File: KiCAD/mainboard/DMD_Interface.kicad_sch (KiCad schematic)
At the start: 21 parts, among them IC3 SN74AUP1G06DCKR, IC4 SN74AUP1G07DCKR, IC5 SN74AUP1G07DCKR, J1 AXT550124, J10 Conn_01x05_Pin, J30 Conn_01x08_Pin

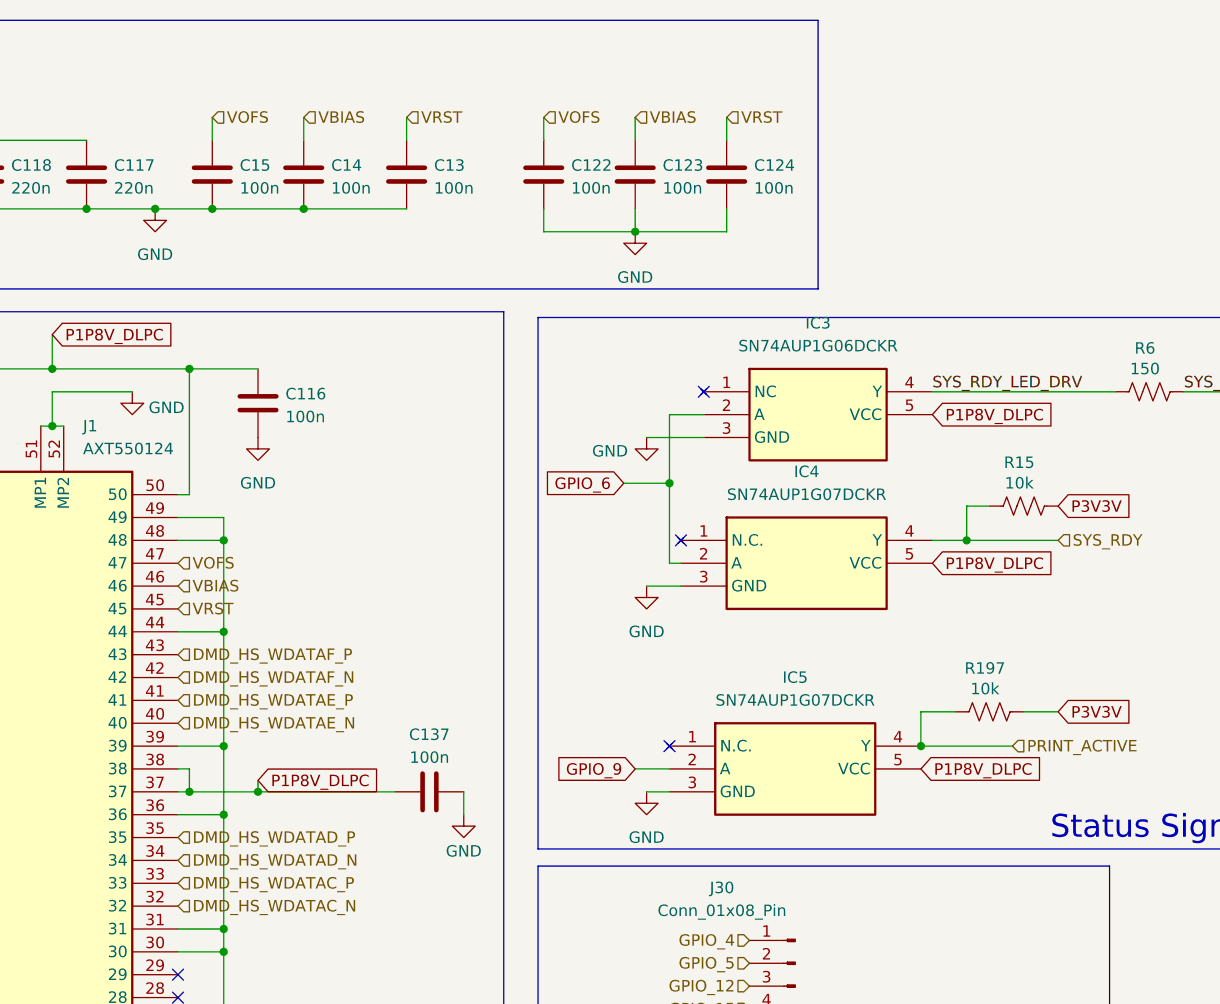
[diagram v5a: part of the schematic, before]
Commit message: replaced with 0805 all passives in DLPC
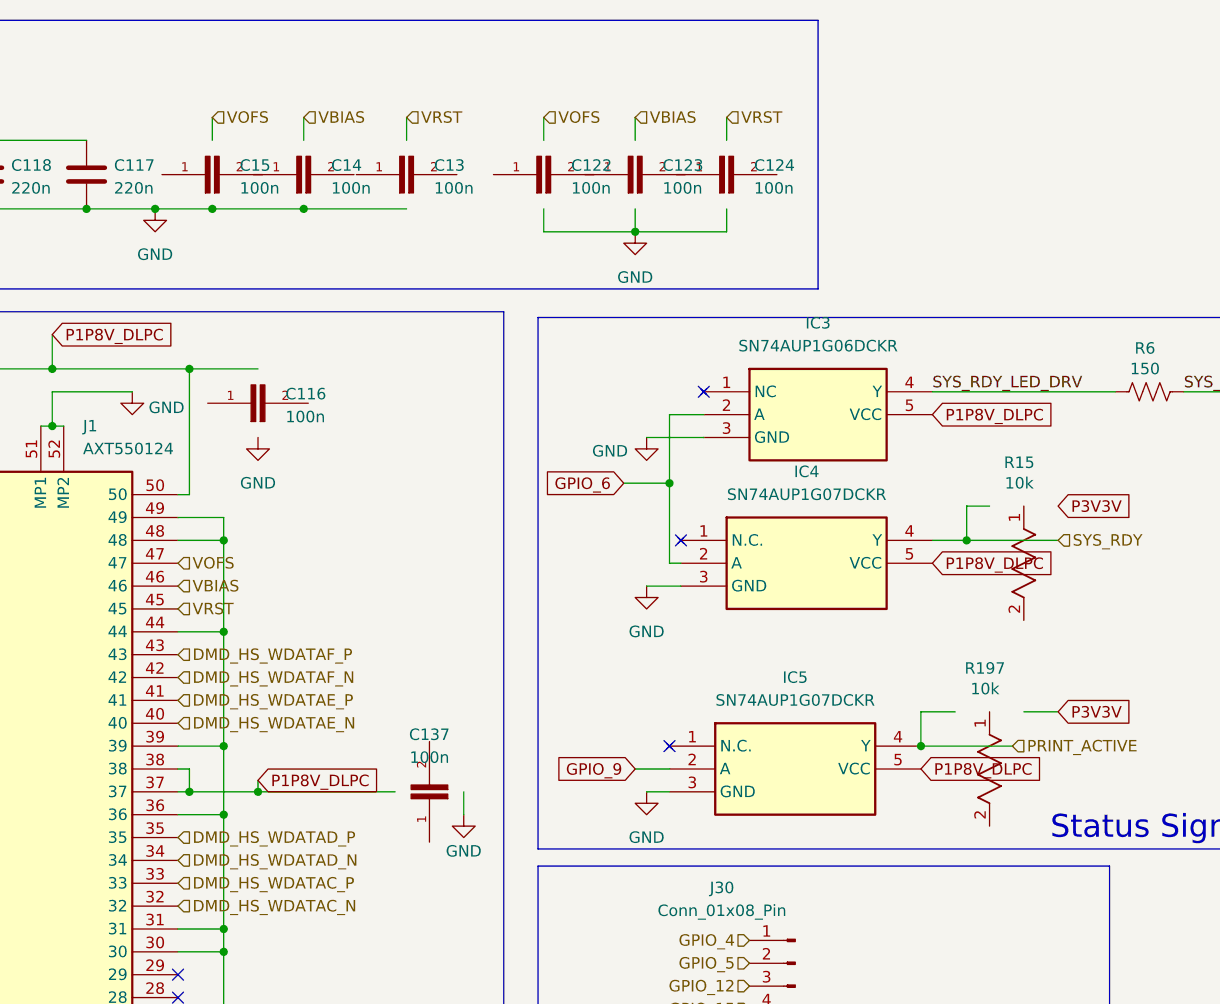
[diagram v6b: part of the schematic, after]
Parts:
- C116, C122, C123, C124, C13, C137, C14, C15: footprint Capacitor_SMD:C_0402_1005Metric -> CC0805KRX7R9BB104:CAPC2012X70; symbol Device:C -> CC0805KRX7R9BB104:CC0805KRX7R9BB104; Check_prices (none) -> https://www.snapeda.com/parts/CC0805KRX7R9BB104/Yageo/view-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; Description_1 (none) -> 0.1 µF ±10% 50V Ceramic Capacitor X7R 0805 (2012 Metric); DigiKey_Part_Number (none) -> 311-1140-1-ND; MANUFACTURER (none) -> YAGEO; MF (none) -> Yageo; MP (none) -> CC0805KRX7R9BB104; Package (none) -> 0805 Yageo; SnapEDA_Link (none) -> https://www.snapeda.com/parts/CC0805KRX7R9BB104/Yageo/view-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
- R15, R197: footprint Resistor_SMD:R_0402_1005Metric -> STA_RMCF0805_STP; symbol Device:R_US -> RMCF0805FT10K0:RMCF0805FT10K0; Manufacturer_Part_Number RC0402FR-0710KL -> RMCF0805FT10K0
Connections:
- net GND: no longer C116.2, C122.2, C123.2, C124.2, C13.2, C137.2, C14.2, C15.2
- net P1P8V_DLPC: no longer C116.1, C137.1
- net P3V3V: no longer R15.1, R197.1
- net PRINT_ACTIVE: no longer R197.2
- net SYS_RDY: no longer R15.2
- net VBIAS: no longer C123.1, C14.1
- net VOFS: no longer C122.1, C15.1
- net VRST: no longer C124.1, C13.1

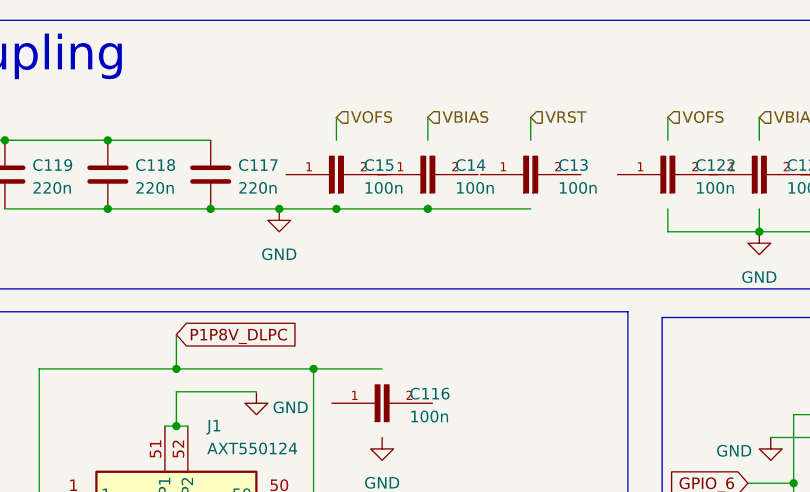
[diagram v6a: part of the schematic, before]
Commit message: capacitors placed back in place
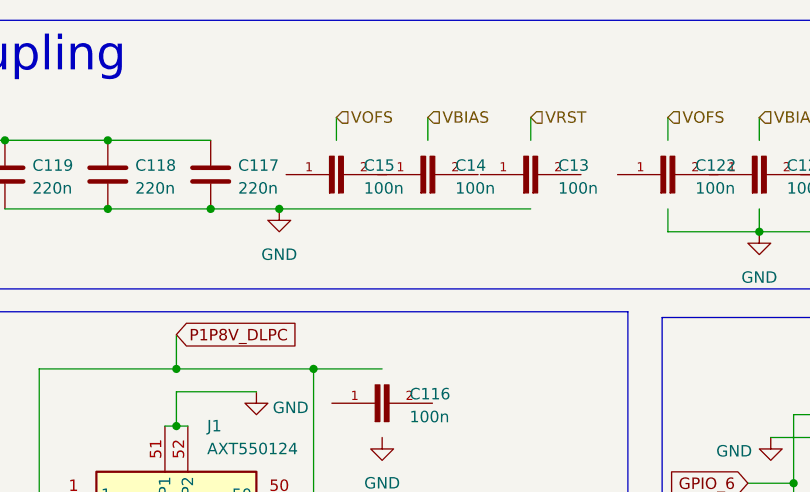
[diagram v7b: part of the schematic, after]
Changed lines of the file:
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@@
-	)
-	(junction
-		(at 83.82 41.91)
-		(diameter 0)
-		(color 0 0 0 0)
 	)
 	(junction
@@
 	(junction
 		(at 124.46 72.39)
-		(diameter 0)
-		(color 0 0 0 0)
-	)
-	(junction
-		(at 73.66 41.91)
 		(diameter 0)
 		(color 0 0 0 0)
@@
 	(wire
 		(pts
-			(xy 83.82 41.91) (xy 95.25 41.91)
-		)
-		(stroke
-			(width 0)
-			(type default)
-		)
-	)
-	(wire
-		(pts
 			(xy 134.62 149.86) (xy 118.11 149.86)
 		)
@@
 	(wire
 		(pts
-			(xy 67.31 41.91) (xy 73.66 41.91)
+			(xy 67.31 41.91) (xy 95.25 41.91)
 		)
 		(stroke
@@
 		)
 		(stroke
-			(width 0)
-			(type default)
-		)
-	)
-	(wire
-		(pts
-			(xy 73.66 41.91) (xy 83.82 41.91)
-		)
-		(stroke

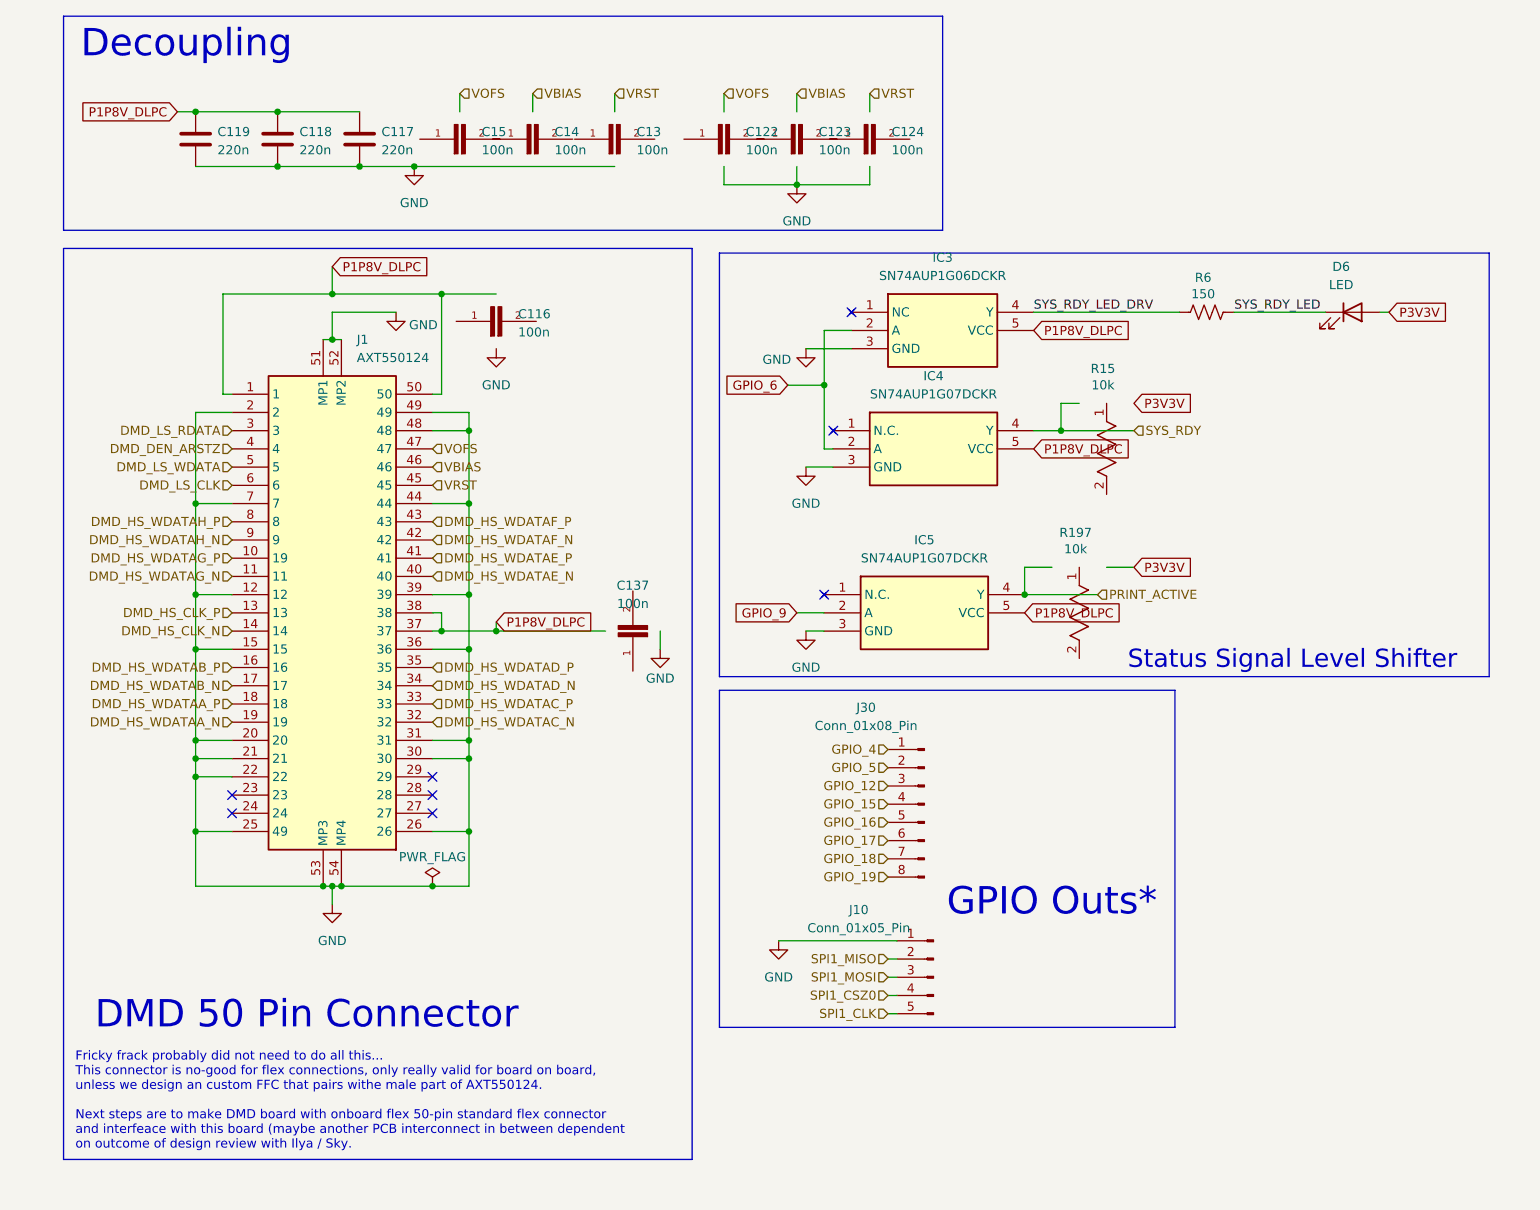
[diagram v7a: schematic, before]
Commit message: changes to all schematic files fixing ERC errors
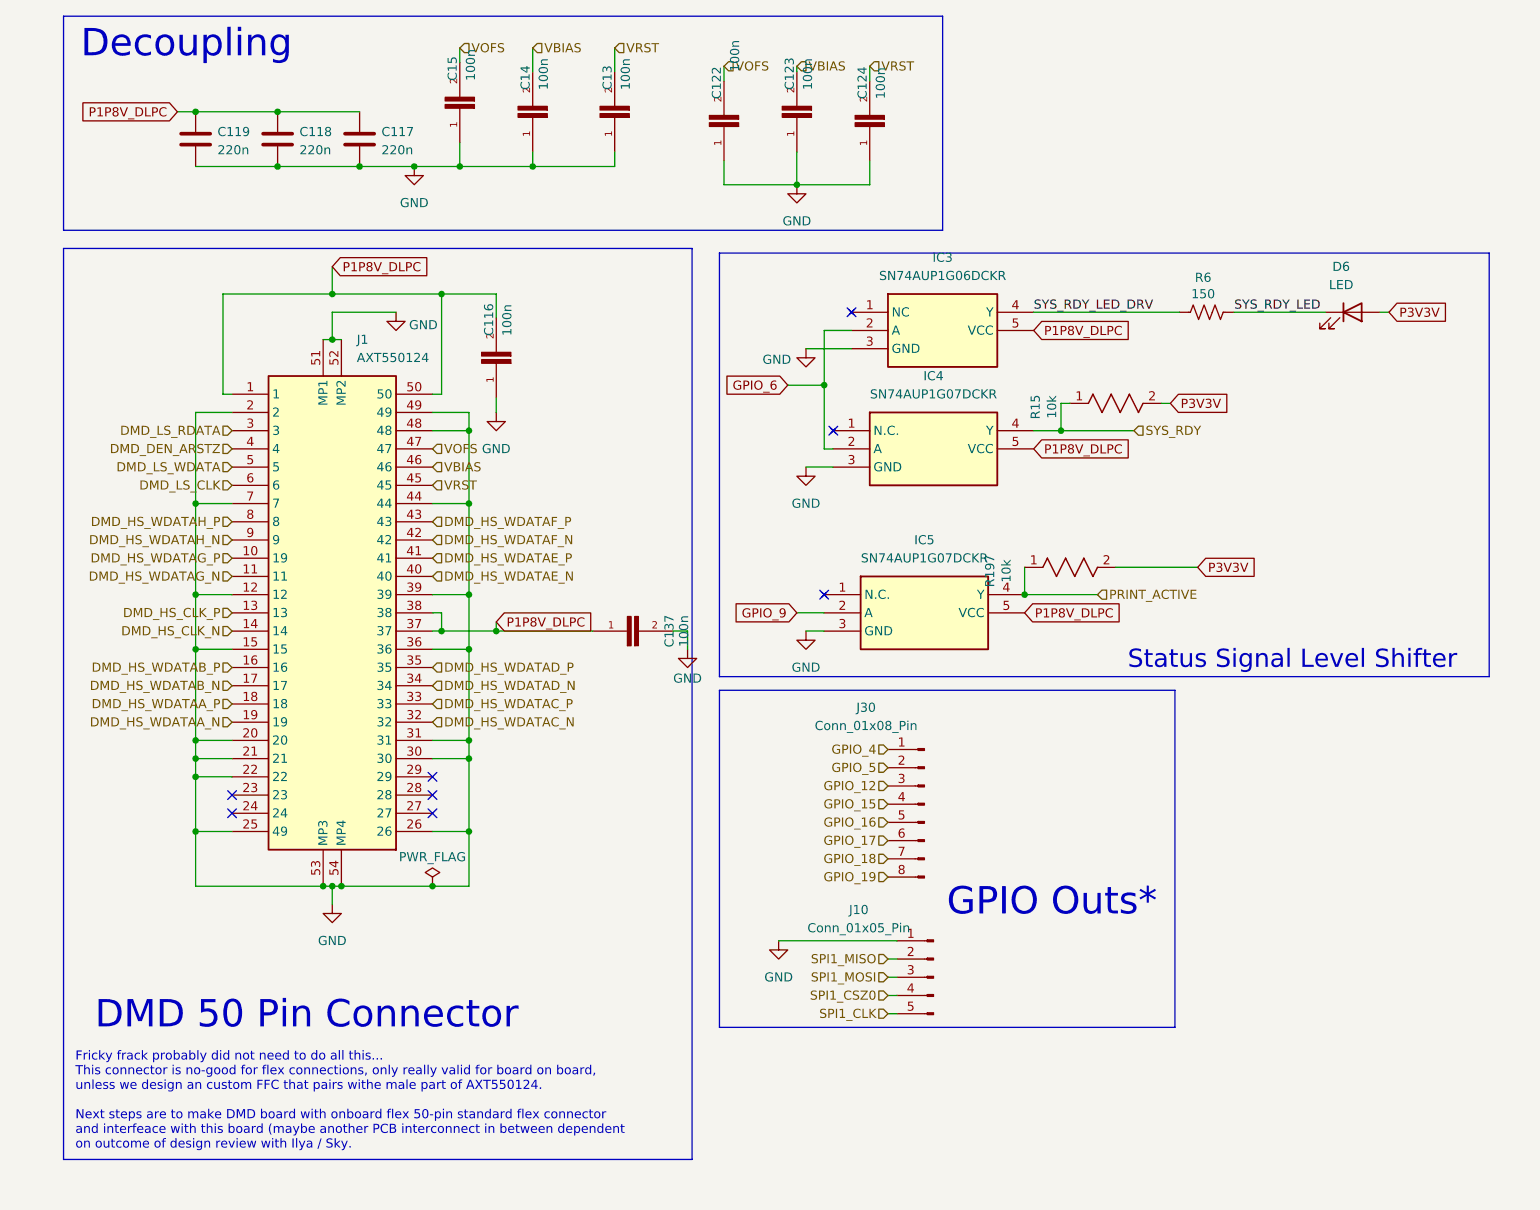
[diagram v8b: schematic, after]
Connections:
- net GND: now also C116.1, C122.1, C123.1, C124.1, C13.1, C137.2, C14.1, C15.1
- net P1P8V_DLPC: now also C116.2, C137.1
- net P3V3V: now also R15.2, R197.2
- net PRINT_ACTIVE: now also R197.1
- net SYS_RDY: now also R15.1
- net VBIAS: now also C123.2, C14.2
- net VOFS: now also C122.2, C15.2
- net VRST: now also C124.2, C13.2
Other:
- moved on the sheet: C116, C122, C123, C124, C13, C137, C14, C15, R15, R197
